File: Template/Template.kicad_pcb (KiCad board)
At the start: 2 copper layers, 85 x 99.5 mm, 19 parts

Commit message: [Template] - updated indicator LED labels on template PCB.
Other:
- board text added: "B0"
- board text added: "B1"
- board text added: "B2"
- board text added: "B3"
- board text added: "B4"
- board text added: "B5"
- board text added: "B6"
- board text added: "B7"
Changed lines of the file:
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@@
 			(at 3.15 0.300052 90)
 			(layer "F.SilkS")
+			(hide yes)
 			(effects
 				(font
@@
 			(at 3.075 0.225104 90)
 			(layer "F.SilkS")
+			(hide yes)
 			(effects
 				(font
@@
 			(at 3.075 0.100208 90)
 			(layer "F.SilkS")
+			(hide yes)
 			(effects
 				(font
@@
 			(at 3.075 0.224948 90)
 			(layer "F.SilkS")
+			(hide yes)
 			(effects
 				(font
@@
 			(at 3.075 0.249845 90)
 			(layer "F.SilkS")
+			(hide yes)
 			(effects
 				(font
@@
 			(at 3.075 0.025156 90)
 			(layer "F.SilkS")
+			(hide yes)
 			(effects
 				(font
@@
 			(at 3.075 0.024896 90)
 			(layer "F.SilkS")
+			(hide yes)
 			(effects
 				(font
@@
 			(at 3.075 0.175 90)
 			(layer "F.SilkS")
+			(hide yes)
 			(effects
 				(font
@@
 			)
 			(justify left bottom)
+		)
+	)
+	(gr_text "B0"
+		(at 45.35 36.65 0)
+		(layer "F.SilkS")
+		(effects
+			(font
+				(size 1.5 1.5)
+				(thickness 0.3)
+				(bold yes)
+			)
+			(justify left bottom)
+		)
+	)
+	(gr_text "B1"
+		(at 50.564286 36.65 0)
+		(layer "F.SilkS")
+		(effects
+			(font
+				(size 1.5 1.5)
+				(thickness 0.3)
+				(bold yes)
+			)
+			(justify left bottom)
+		)
+	)
+	(gr_text "B2"
+		(at 55.778571 36.65 0)
+		(layer "F.SilkS")
+		(effects
+			(font
+				(size 1.5 1.5)
+				(thickness 0.3)
+				(bold yes)
+			)
+			(justify left bottom)
+		)
+	)
+	(gr_text "B3"
+		(at 60.992857 36.65 0)
+		(layer "F.SilkS")
+		(effects
+			(font
+				(size 1.5 1.5)
+				(thickness 0.3)
+				(bold yes)
+			)
+			(justify left bottom)
+		)
+	)
+	(gr_text "B4"
+		(at 66.207143 36.65 0)
+		(layer "F.SilkS")
+		(effects
+			(font
+				(size 1.5 1.5)
+				(thickness 0.3)
+				(bold yes)
+			)
+			(justify left bottom)
+		)
+	)
+	(gr_text "B5"
+		(at 71.421429 36.65 0)
+		(layer "F.SilkS")
+		(effects
+			(font
+				(size 1.5 1.5)
+				(thickness 0.3)
+				(bold yes)
+			)
+			(justify left bottom)
+		)
+	)
+	(gr_text "B6"
+		(at 76.635714 36.65 0)
+		(layer "F.SilkS")
+		(effects
+			(font
+				(size 1.5 1.5)
+				(thickness 0.3)
+				(bold yes)
+			)
+			(justify left bottom)
+		)
+	)
+	(gr_text "B7"
+		(at 81.85 36.65 0)
+		(layer "F.SilkS")
+		(effects
+			(font
+				(size 1.5 1.5)
+				(thickness 0.3)
+				(bold yes)
+			)
+			(justify left bottom)

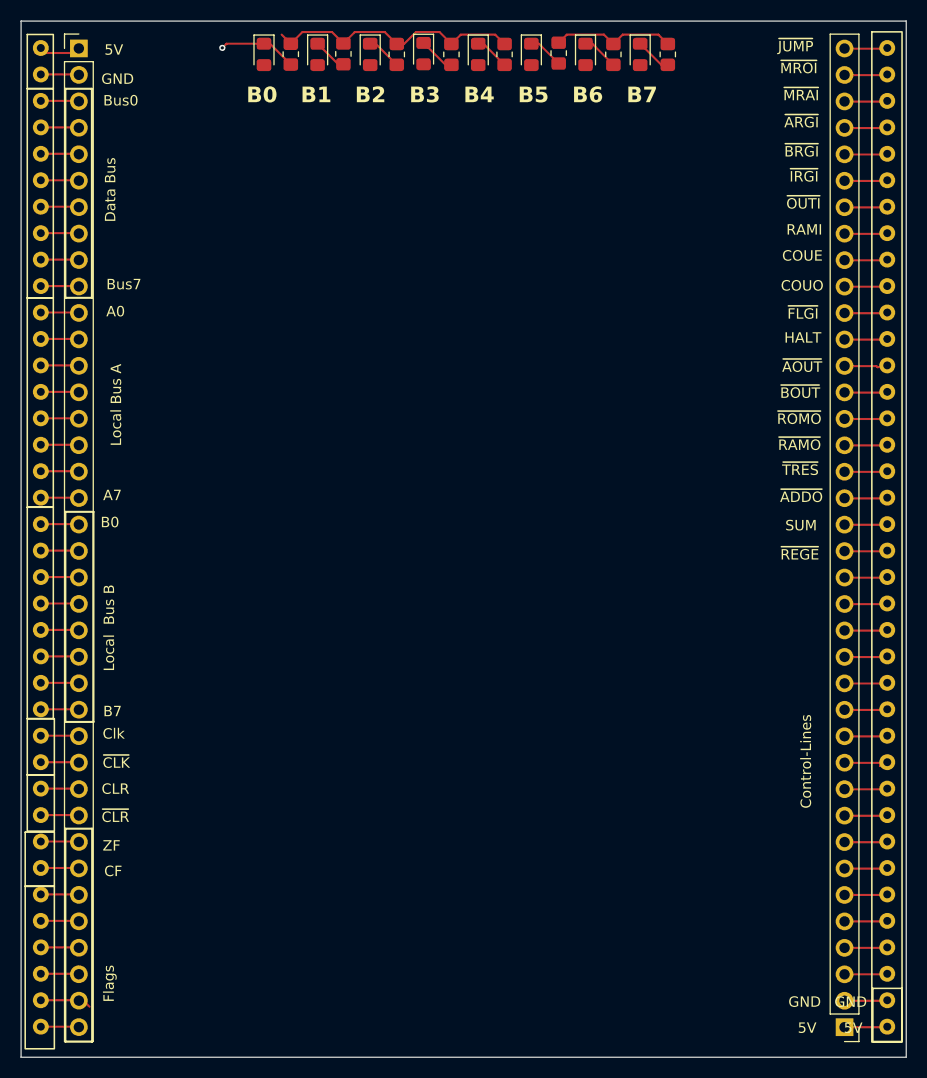
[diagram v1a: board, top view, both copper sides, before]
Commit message: [Template] - fixed annoying DRC errors with silkscreen. Added second set of carry and zero flags.
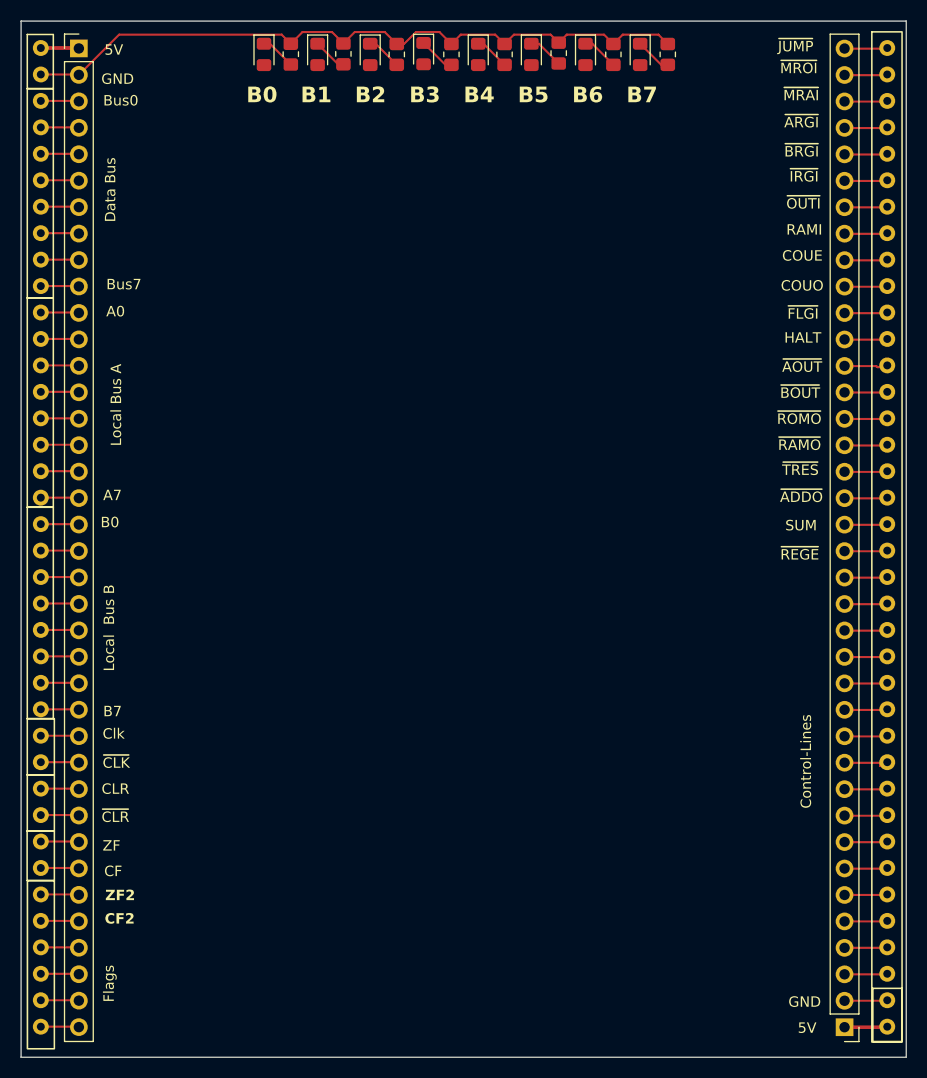
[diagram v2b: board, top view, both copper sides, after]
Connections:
- net FL-2 renamed ZFLAG2
- net FL-3 renamed CFLAG2
- net ZFLG renamed ZFLAG
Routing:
- net GND: track 45.3 -> 72.2 mm
- net Net-(D8-K): track 7.57 -> 3.40 mm, vias 1 -> 0
- net 5V: track 9.15 -> 8.61 mm
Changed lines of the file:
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@@
 	)
 	(setup
+		(stackup
+			(layer "F.SilkS"
+				(type "Top Silk Screen")
+			)
+			(layer "F.Paste"
+				(type "Top Solder Paste")
+			)
+			(layer "F.Mask"
+				(type "Top Solder Mask")
+				(thickness 0.01)
+			)
+			(layer "F.Cu"
+				(type "copper")
+				(thickness 0.035)
+			)
+			(layer "dielectric 1"
+				(type "core")
+				(thickness 1.51)
+				(material "FR4")
+				(epsilon_r 4.5)
+				(loss_tangent 0.02)
+			)
+			(layer "B.Cu"
+				(type "copper")
+				(thickness 0.035)
+			)
+			(layer "B.Mask"
+				(type "Bottom Solder Mask")
+				(thickness 0.01)
+			)
+			(layer "B.Paste"
+				(type "Bottom Solder Paste")
+			)
+			(layer "B.SilkS"
+				(type "Bottom Silk Screen")
+			)
+			(copper_finish "None")
+			(dielectric_constraints no)
+		)
 		(pad_to_mask_clearance 0)
 		(allow_soldermask_bridges_in_footprints no)
@@
 		(capping no)
 		(filling no)
+		(zone_defaults)
 		(pcbplotparams
 			(layerselection 0x00000000_00000000_55555555_5755f5ff)
@@
 		(duplicate_pad_numbers_are_jumpers no)
 		(fp_rect
-			(start -41.3 39.1)
-			(end -38.5 44.3)
-			(stroke
-				(width 0.15)
-				(type default)
-			)
-			(fill no)
-			(layer "F.SilkS")
-		)
-		(fp_rect
-			(start -41.3 44.3)
-			(end -38.5 59.9)
+			(start -41.11481 39)
+			(end -38.5 43.75)
 			(stroke
 				(width 0.15)
@@
 		)
 		(fp_rect
+			(start -41.084792 43.75)
+			(end -38.5 59.9)
+			(stroke
+				(width 0.15)
+				(type default)
+			)
+			(fill no)
+			(layer "F.SilkS")
+		)
+		(fp_rect
 			(start 40 -37.75)
 			(end 42.9 59.25)
@@
 			)
 		)
+		(fp_text user "CF2"
+			(at -33.67 48 0)
+			(unlocked yes)
+			(layer "F.SilkS")
+			(effects
+				(font
+					(size 1 1)
+					(thickness 0.2)
+					(bold yes)
+				)
+				(justify left bottom)
+			)
+		)
+		(fp_text user "ZF2"
+			(at -33.62 45.75 0)
+			(unlocked yes)
+			(layer "F.SilkS")
+			(effects
+				(font
+					(size 1 1)
+					(thickness 0.2)
+					(bold yes)
+				)
+				(justify left bottom)
+			)
+		)
 		(fp_text user "Bus7"
 			(at -33.52 -12.91 0)
@@
 			(at 36.4 56 0)
 			(unlocked yes)
-			(layer "F.SilkS")
+			(layer "F.Fab")
 			(effects
 				(font
@@
 			(at 37.3 58.5 0)
 			(unlocked yes)
-			(layer "F.SilkS")
+			(layer "F.Fab")
 			(effects
 				(font
@@
 			(layers "*.Cu" "*.Mask")
 			(remove_unused_layers no)
-			(net "ZFLG")
+			(net "ZFLAG")
 			(pinfunction "ZFlag_31")
 			(pintype "bidirectional")
@@
 			(layers "*.Cu" "*.Mask")
 			(remove_unused_layers no)
-			(net "FL-2")
-			(pinfunction "FL-2_33")
+			(net "ZFLAG2")
+			(pinfunction "ZFlag2_33")
 			(pintype "bidirectional")
 		)
@@
 			(layers "*.Cu" "*.Mask")
 			(remove_unused_layers no)
-			(net "FL-3")
-			(pinfunction "FL-3_34")
+			(net "CFLAG2")
+			(pinfunction "CFlag2_34")
 			(pintype "bidirectional")
 		)
@@
 			(layers "*.Cu" "*.Mask")
 			(remove_unused_layers no)
-			(net "ZFLG")
+			(net "ZFLAG")
 			(pinfunction "ZFlag_31")
 			(pintype "bidirectional")
@@
 			(layers "*.Cu" "*.Mask")
 			(remove_unused_layers no)
-			(net "FL-2")
+			(net "ZFLAG2")
 			(pinfunction "FL-2_33")
 			(pintype "bidirectional")
@@
 			(layers "*.Cu" "*.Mask")
 			(remove_unused_layers no)
-			(net "FL-3")
+			(net "CFLAG2")
 			(pinfunction "FL-3_34")
 			(pintype "bidirectional")
@@
 	)
 	(gr_rect
-		(start 27.975 35.175)
-		(end 30.525 55.25)
-		(stroke
-			(width 0.2)
-			(type default)
-		)
-		(fill no)
-		(layer "F.SilkS")
-	)
-	(gr_rect
-		(start 27.975 75.8)
-		(end 30.675 95.975)
-		(stroke
-			(width 0.2)
-			(type default)
-		)
-		(fill no)
-		(layer "F.SilkS")
-	)
-	(gr_rect
-		(start 27.975 106.225)
-		(end 30.55 126.675)
-		(stroke
-			(width 0.2)
-			(type default)
-		)
-		(fill no)
-		(layer "F.SilkS")
-	)
-	(gr_rect
 		(start 23.725 28.675)
 		(end 108.725 128.175)
@@
 	)
 	(segment
+		(start 74.575 29.975)
+		(end 71.050052 29.975)
+		(width 0.2)
+		(layer "F.Cu")
+		(net "GND")
+	)
+	(segment
 		(start 69.250052 29.975)
 		(end 70.150052 30.875)
@@
 	)
 	(segment
+		(start 71.050052 29.975)
+		(end 70.150052 30.875)
+		(width 0.2)
+		(layer "F.Cu")
+		(net "GND")
+	)
+	(segment
 		(start 58.650156 29.725)
 		(end 59.800156 30.875)
@@
 	)
 	(segment
+		(start 75.35 30.75)
+		(end 74.575 29.975)
+		(width 0.2)
+		(layer "F.Cu")
+		(net "GND")
+	)
+	(segment
 		(start 55.775208 29.725)
 		(end 58.650156 29.725)
@@
 	)
 	(segment
+		(start 29.275 33.84)
+		(end 33.14 29.975)
+		(width 0.2)
+		(layer "F.Cu")
+		(net "GND")
+	)
+	(segment
 		(start 61.650156 29.725)
 		(end 63.900104 29.725)
@@
 	)
 	(segment
+		(start 33.14 29.975)
+		(end 48.75026 29.975)
+		(width 0.2)
+		(layer "F.Cu")
+		(net "GND")
+	)
+	(segment
 		(start 79.699948 29.975)
 		(end 80.599948 30.875)
@@
 	)
 	(segment
-		(start 47.05026 30.85)
-		(end 43.45 30.85)
-		(width 0.2)
-		(layer "F.Cu")
-		(net "Net-(D8-K)")
-	)
-	(segment
-		(start 43.45 30.85)
-		(end 43.05 31.25)
-		(width 0.2)
-		(layer "F.Cu")
-		(net "Net-(D8-K)")
-	)
-	(segment
 		(start 47.62526 30.85)
 		(end 49.62526 32.85)
@@
 		(net "Net-(D8-K)")
 	)
-	(via
-		(at 43.05 31.25)
-		(size 0.6)
-		(drill 0.3)
-		(layers "F.Cu" "B.Cu")
-		(net "Net-(D8-K)")
-	)
 	(segment
 		(start 25.115 31.74)
@@
 	)
 	(segment
-		(start 102.8 125.29)
-		(end 106.85 125.29)
-		(width 0.2)
+		(start 106.85 125.29)
+		(end 106.9 125.24)
+		(width 0.35)
 		(layer "F.Cu")
 		(net "5V")
 	)
 	(segment
-		(start 29.325 31.74)
-		(end 25.115 31.74)
+		(start 25.43 31.425)
+		(end 25.8 31.425)
 		(width 0.2)
 		(layer "F.Cu")
@@
 	)
 	(segment
-		(start 25.43 31.425)
-		(end 25.8 31.425)
-		(width 0.2)
+		(start 102.8 125.29)
+		(end 106.85 125.29)
+		(width 0.35)
 		(layer "F.Cu")
 		(net "5V")
 	)
 	(segment
-		(start 106.85 125.29)
-		(end 106.9 125.24)
-		(width 0.2)
+		(start 25.62 31.26)
+		(end 29.235 31.26)
+		(width 0.35)
+		(layer "F.Cu")
+		(net "5V")
+	)
+	(segment
+		(start 29.235 31.26)
+		(end 29.275 31.3)
+		(width 0.35)
 		(layer "F.Cu")
 		(net "5V")
@@
 	)
 	(segment
-		(start 25.62 107.46)
-		(end 28.845 107.46)
-		(width 0.2)
-		(layer "F.Cu")
-		(net "ZFLG")
-	)
-	(segment
-		(start 28.845 107.46)
-		(end 29.325 107.94)
-		(width 0.2)
-		(layer "F.Cu")
-		(net "ZFLG")
-	)
-	(segment
 		(start 28.845 110)
 		(end 29.325 110.48)
@@
 	)
 	(segment
-		(start 25.62 112.54)
-		(end 28.845 112.54)
-		(width 0.2)
-		(layer "F.Cu")
-		(net "FL-2")
-	)
-	(segment
-		(start 28.845 112.54)
-		(end 29.325 113.02)
-		(width 0.2)
-		(layer "F.Cu")
-		(net "FL-2")
-	)
-	(segment
-		(start 28.845 115.08)
-		(end 29.325 115.56)
-		(width 0.2)
-		(layer "F.Cu")
-		(net "FL-3")
-	)
-	(segment
-		(start 25.62 115.08)
-		(end 28.845 115.08)
-		(width 0.2)
-		(layer "F.Cu")
-		(net "FL-3")
-	)
-	(segment
 		(start 25.62 117.62)
 		(end 28.845 117.62)
@@
 	)
 	(segment
-		(start 30.29 123.315)
-		(end 29.975 123)
-		(width 0.2)
-		(layer "F.Cu")
-		(net "FL-6")
-	)
-	(segment
 		(start 28.845 122.7)
 		(end 29.325 123.18)
@@
 		(net "Net-(D7-K)")
 	)
+	(segment
+		(start 25.62 107.46)
+		(end 28.845 107.46)
+		(width 0.2)
+		(layer "F.Cu")
+		(net "ZFLAG")
+	)
+	(segment
+		(start 28.845 107.46)
+		(end 29.325 107.94)
+		(width 0.2)
+		(layer "F.Cu")
+		(net "ZFLAG")
+	)
+	(segment
+		(start 28.845 115.08)
+		(end 29.325 115.56)
+		(width 0.2)
+		(layer "F.Cu")
+		(net "CFLAG2")
+	)
+	(segment
+		(start 25.62 115.08)
+		(end 28.845 115.08)
+		(width 0.2)
+		(layer "F.Cu")
+		(net "CFLAG2")
+	)
+	(segment
+		(start 25.62 112.54)
+		(end 28.845 112.54)
+		(width 0.2)
+		(layer "F.Cu")
+		(net "ZFLAG2")
+	)
+	(segment
+		(start 28.845 112.54)
+		(end 29.325 113.02)
+		(width 0.2)
+		(layer "F.Cu")
+		(net "ZFLAG2")
+	)
 	(embedded_fonts no)

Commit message: [Template] - updated for COUO being inverted signal  Please enter the commit message for your changes. Lines starting
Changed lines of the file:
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@@
 		(capping no)
 		(filling no)
-		(zone_defaults)
 		(pcbplotparams
 			(layerselection 0x00000000_00000000_55555555_5755f5ff)
@@
 			)
 		)
-		(fp_text user "COUO"
+		(fp_text user "~{COUO}"
 			(at 31.255 -12.785 0)
 			(unlocked yes)
@@
 	)
 	(segment
+		(start 25.62 107.46)
+		(end 28.845 107.46)
+		(width 0.2)
+		(layer "F.Cu")
+		(net "ZFLAG")
+	)
+	(segment
+		(start 28.845 107.46)
+		(end 29.325 107.94)
+		(width 0.2)
+		(layer "F.Cu")
+		(net "ZFLAG")
+	)
+	(segment
 		(start 28.845 110)
 		(end 29.325 110.48)
@@
 	)
 	(segment
+		(start 25.62 112.54)
+		(end 28.845 112.54)
+		(width 0.2)
+		(layer "F.Cu")
+		(net "ZFLAG2")
+	)
+	(segment
+		(start 28.845 112.54)
+		(end 29.325 113.02)
+		(width 0.2)
+		(layer "F.Cu")
+		(net "ZFLAG2")
+	)
+	(segment
+		(start 28.845 115.08)
+		(end 29.325 115.56)
+		(width 0.2)
+		(layer "F.Cu")
+		(net "CFLAG2")
+	)
+	(segment
+		(start 25.62 115.08)
+		(end 28.845 115.08)
+		(width 0.2)
+		(layer "F.Cu")
+		(net "CFLAG2")
+	)
+	(segment
 		(start 25.62 117.62)
 		(end 28.845 117.62)
@@
 		(net "Net-(D7-K)")
 	)
-	(segment
-		(start 25.62 107.46)
-		(end 28.845 107.46)
-		(width 0.2)
-		(layer "F.Cu")
-		(net "ZFLAG")
-	)
-	(segment
-		(start 28.845 107.46)
-		(end 29.325 107.94)
-		(width 0.2)
-		(layer "F.Cu")
-		(net "ZFLAG")
-	)
-	(segment
-		(start 28.845 115.08)
-		(end 29.325 115.56)
-		(width 0.2)
-		(layer "F.Cu")
-		(net "CFLAG2")
-	)
-	(segment
-		(start 25.62 115.08)
-		(end 28.845 115.08)
-		(width 0.2)
-		(layer "F.Cu")
-		(net "CFLAG2")
-	)
-	(segment
-		(start 25.62 112.54)
-		(end 28.845 112.54)
-		(width 0.2)
-		(layer "F.Cu")
-		(net "ZFLAG2")
-	)
-	(segment
-		(start 28.845 112.54)
-		(end 29.325 113.02)
-		(width 0.2)
-		(layer "F.Cu")
-		(net "ZFLAG2")
-	)
 	(embedded_fonts no)
